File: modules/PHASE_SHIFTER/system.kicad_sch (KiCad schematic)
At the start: 2 parts, among them J1 Card_Connector

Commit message: started phase shifter
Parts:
- added C10, C11: 10µ, FormantKO:CP_Axial_600, symbol FormantKO:C_Polarized
- added D1: ${SIM.PARAMS}, FormantKO:DUZ, symbol FormantKO:DUZ
- added D2: 12V, FormantKO:DUZ, symbol FormantKO:DUZ
- added IC1, IC2: LM324, FormantKO:DIP-14, symbol FormantKO:LM324
- added R37, R38: 150R, FormantKO:R_Axial_Horizontal, symbol FormantKO:R
- MH1: value (none) -> CardBracket; footprint FormantKO:Schroff_60807-011_3U_Pair -> FormantKO:Card_Bracket
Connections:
- net +15V: now also R37.2
- net -15V: now also R38.1
- net GND: now also C10.2, C11.1, D1.2 (A+), D2.1 (K-)
- new net +12V: C10.1, D1.1 (K-), IC1.4 (V+), IC2.4 (V+), R37.1
- new net -12V: C11.2, D2.2 (A+), IC1.11 (V-), IC2.11 (V-), R38.2
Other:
- title: TEMPLATE -> PHASE-SHIFTER

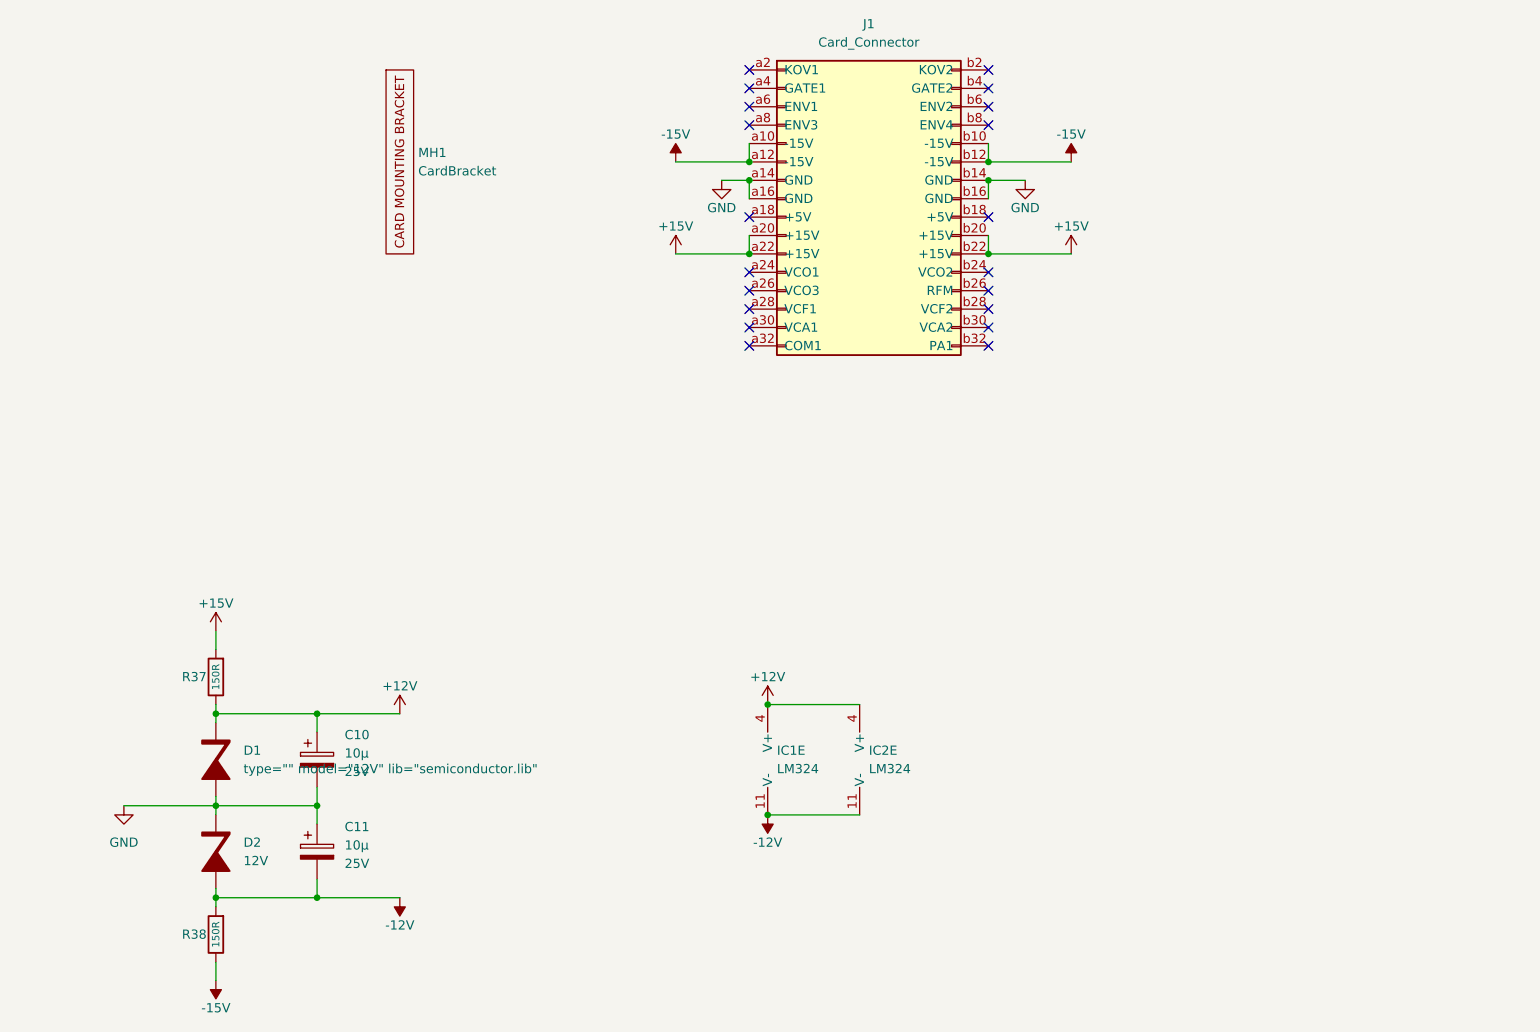
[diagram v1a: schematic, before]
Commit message: phase shifter pcb placement
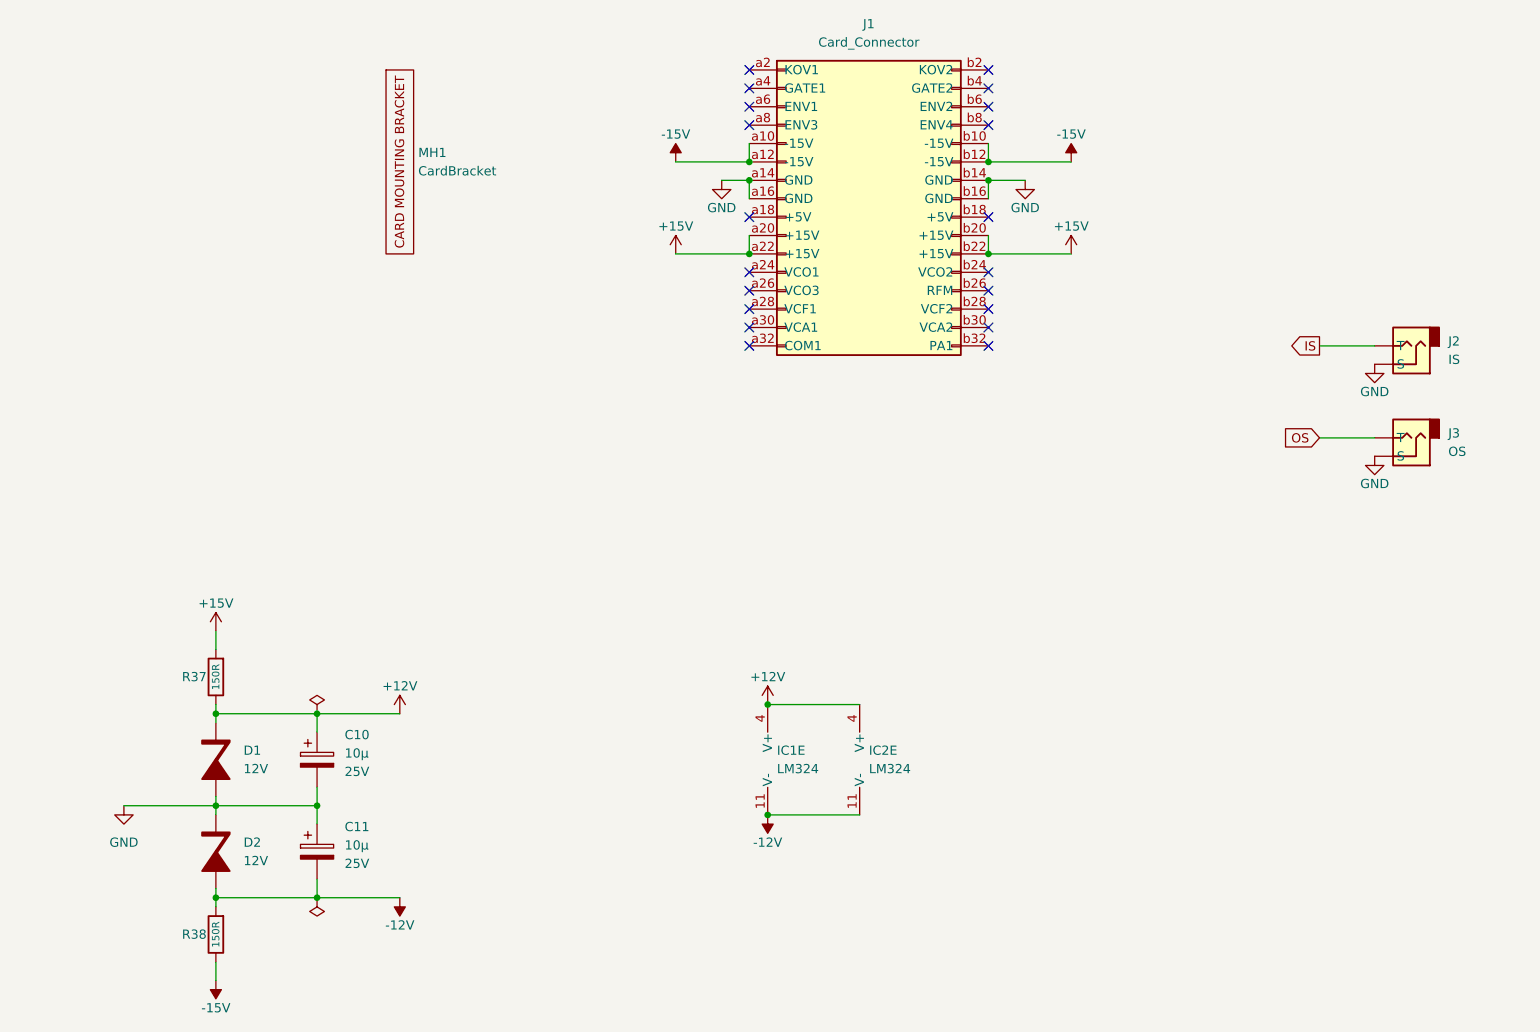
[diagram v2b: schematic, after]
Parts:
- added J2: IS, FormantKO:PanelConnector_1x02, symbol FormantKO:MonoJack
- added J3: OS, FormantKO:PanelConnector_1x02, symbol FormantKO:MonoJack
- D1: value ${SIM.PARAMS} -> 12V
- J1: footprint FormantKO:Card_Connector -> FormantKO:CardConnector; symbol FormantKO:Card_Connector -> FormantKO:CardConnector
- MH1: footprint FormantKO:Card_Bracket -> FormantKO:CardBracket; symbol FormantKO:Card_Bracket -> FormantKO:CardBracket
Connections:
- net GND: now also J2.1 (S), J3.1 (S)
- new net IS: J2.2 (T)
- new net OS: J3.2 (T)

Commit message: phase shifter trace work
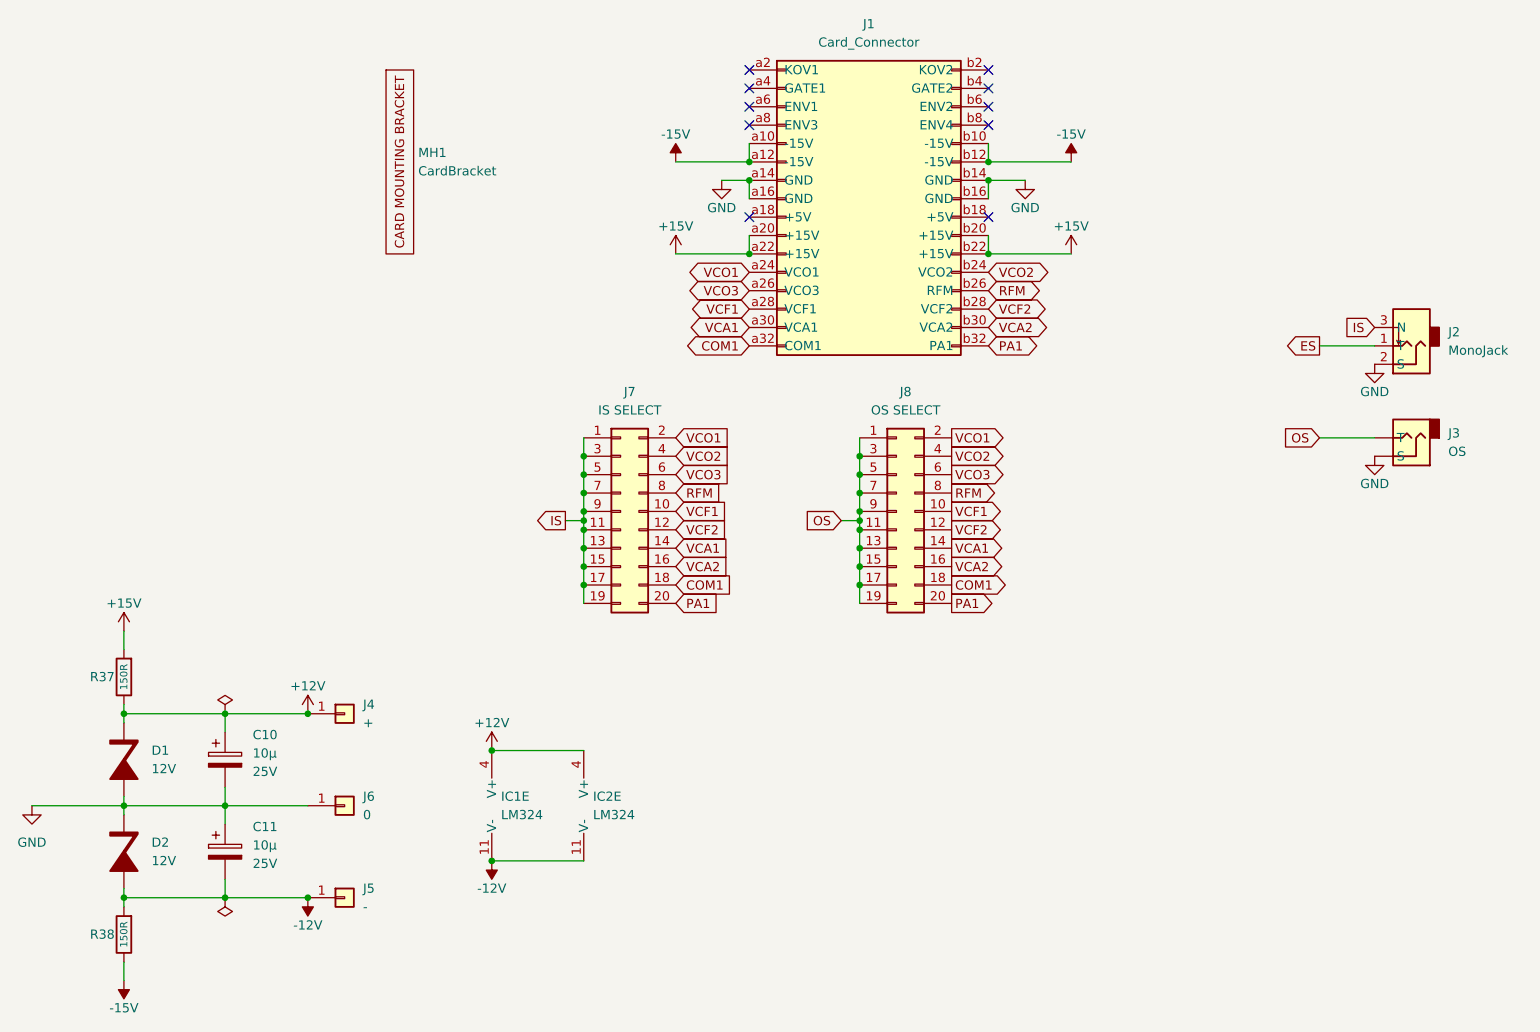
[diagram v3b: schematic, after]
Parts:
- removed J2: IS, FormantKO:PanelConnector_1x02, symbol FormantKO:MonoJack
- added J2: MonoJack, FormantKO:PanelConnector_1x03, symbol FormantKO:MonoJack_Switched
- added J4: +, FormantKO:Wire_1x01_General, symbol FormantKO:Wire_1x01
- added J5: -, FormantKO:Wire_1x01_General, symbol FormantKO:Wire_1x01
- added J6: 0, FormantKO:Wire_1x01_General, symbol FormantKO:Wire_1x01
- added J7: IS SELECT, Connector_PinHeader_2.54mm:PinHeader_2x10_P2.54mm_Vertical, symbol Connector_Generic:Conn_02x10_Odd_Even
- added J8: OS SELECT, Connector_PinHeader_2.54mm:PinHeader_2x10_P2.54mm_Vertical, symbol Connector_Generic:Conn_02x10_Odd_Even
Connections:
- net +12V: now also J4.1 (Pin_1)
- net -12V: now also J5.1 (Pin_1)
- net GND: now also J2.2 (S), J6.1 (Pin_1)
- net IS: now also J2.3 (N), J7.1 (Pin_1), J7.11 (Pin_11), J7.13 (Pin_13), J7.15 (Pin_15), J7.17 (Pin_17), J7.19 (Pin_19), J7.3 (Pin_3), J7.5 (Pin_5), J7.7 (Pin_7), J7.9 (Pin_9)
- net OS: now also J8.1 (Pin_1), J8.11 (Pin_11), J8.13 (Pin_13), J8.15 (Pin_15), J8.17 (Pin_17), J8.19 (Pin_19), J8.3 (Pin_3), J8.5 (Pin_5), J8.7 (Pin_7), J8.9 (Pin_9)
- net VCO1: now reaches J1.a24 (VCO1)
- net VCO1: now also J7.2 (Pin_2), J8.2 (Pin_2)
- net VCO3: now reaches J1.a26 (VCO3)
- net VCO3: now also J7.6 (Pin_6), J8.6 (Pin_6)
- net VCF1: now reaches J1.a28 (VCF1)
- net VCF1: now also J7.10 (Pin_10), J8.10 (Pin_10)
- net VCA1: now reaches J1.a30 (VCA1)
- net VCA1: now also J7.14 (Pin_14), J8.14 (Pin_14)
- net COM1: now reaches J1.a32 (COM1)
- net COM1: now also J7.18 (Pin_18), J8.18 (Pin_18)
- net VCO2: now reaches J1.b24 (VCO2)
- net VCO2: now also J7.4 (Pin_4), J8.4 (Pin_4)
- net RFM: now reaches J1.b26 (RFM)
- net RFM: now also J7.8 (Pin_8), J8.8 (Pin_8)
- net VCF2: now reaches J1.b28 (VCF2)
- net VCF2: now also J7.12 (Pin_12), J8.12 (Pin_12)
- net VCA2: now reaches J1.b30 (VCA2)
- net VCA2: now also J7.16 (Pin_16), J8.16 (Pin_16)
- net PA1: now reaches J1.b32 (PA1)
- net PA1: now also J7.20 (Pin_20), J8.20 (Pin_20)
- new net ES: J2.1 (T)
- no-connect marks 20 -> 10
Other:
- moved on the sheet: C10, C11, D1, D2, IC1E, IC2E, R37, R38

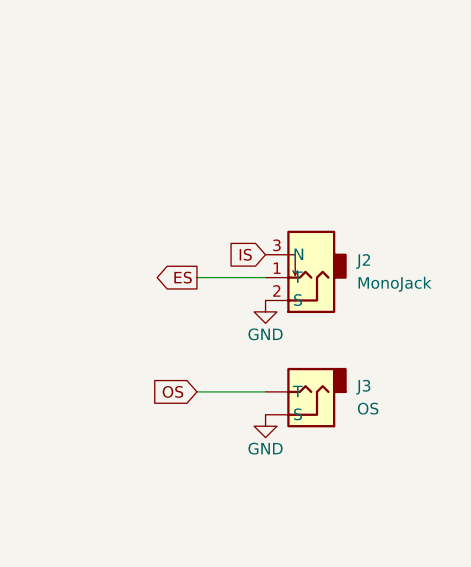
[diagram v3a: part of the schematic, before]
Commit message: phase shifter module ready for proto
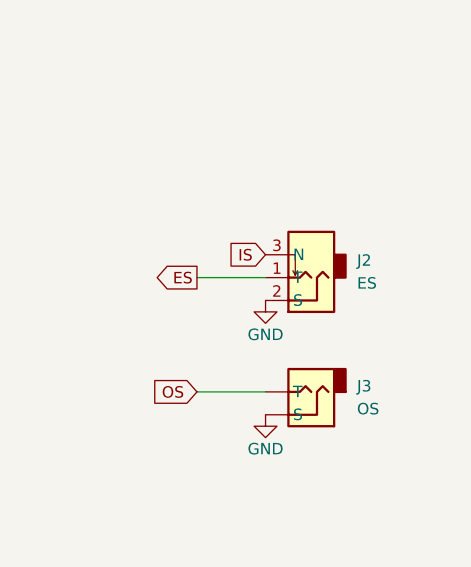
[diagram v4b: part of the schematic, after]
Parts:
- J2: value MonoJack -> ES
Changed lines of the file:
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@@
 			)
 		)
-		(property "Value" "MonoJack"
+		(property "Value" "ES"
 			(at 220.98 89.5349 0)
 			(show_name no)
